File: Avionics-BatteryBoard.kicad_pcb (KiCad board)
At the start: 4 copper layers, 90.2 x 95.9 mm, 148 parts, among them J1 Keystone-1048, J2 Keystone-1048, J3 Keystone-1042, J4 Keystone-1042, J5 Fuel Gauge Programming Header, J6 205338-0002, J7 205338-0004, J8 282834-4, J9 522711069, Q1 SIRA99DP-T1-GE3, Q10 SIRA99DP-T1-GE3, Q11 MBT2222ADW1T1, Q12 NX3008NBKS, Q13 MBT2222ADW1T1, Q14 NX3008NBKS, Q2 IRLML2803, Q3 SIRA99DP-T1-GE3, Q4 IRLML2803, Q5 SIRA99DP-T1-GE3, Q6 IRLML2803, Q7 SIRA99DP-T1-GE3, Q8 SIRA99DP-T1-GE3, Q9 SIRA99DP-T1-GE3, U1 S-8209AAA-T8T1U, U10 TLX9000, U2 S-8209AAA-T8T1U, U3 LTC4412xS6, U4 LTC4412xS6, U5 MAX17205, U6 D5V0P4UR6SO, U7 D5V0P4UR6SO, U8 TLX9000, U9 TLX9000

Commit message: More v3.2 updates
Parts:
- H1, H2, H3, H4: footprint MountingHole:MountingHole_3.2mm_M3_Pad_TopBottom -> MountingHole:MountingHole_3.2mm_M3_Pad_Via
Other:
- outline, holes or cut-outs redrawn
- board text added: "TR"

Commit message: temporary changes
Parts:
- removed D1, D2: BAT60JFILM, Diode_SMD:D_SOD-323_HandSoldering
- removed F1, F2, F3, F4, F5, F6: 5A, Fuse:Fuse_1206_3216Metric
- removed J1, J2: Keystone-1048, Argus-Misc:BAT_1048
- removed J3, J4: Keystone-1042, Argus-Misc:Keystone_1042
- removed R21, R22, R23, R34, R35, R36: 10R, Resistor_SMD:R_2512_6332Metric
- added D7: BAT60JFILM, Diode_SMD:D_SOD-323_HandSoldering, F.Cu at (205.7, 122.5)
- added D8: BAT60JFILM, Diode_SMD:D_SOD-323_HandSoldering, F.Cu at (205.7, 125.4)
- added F12: 5A, Fuse:Fuse_1206_3216Metric, F.Cu at (200.3, 122.7)
- added F13: 5A, Fuse:Fuse_1206_3216Metric, F.Cu at (200.3, 126.0)
- added F14: 5A, Fuse:Fuse_1206_3216Metric, F.Cu at (200.3, 129.3)
- added F15: 5A, Fuse:Fuse_1206_3216Metric, F.Cu at (200.3, 132.6)
- added J11: ~, Argus-Battery:21700_battery_holder_th, F.Cu at (214.7, 139.5)
- TH1, TH6: moved to F.Cu
- moved R30 73.3 mm to (107.1, 68.2), turned to -90 degrees
- moved R29 50.3 mm to (107.1, 84.7), turned to -90 degrees
- moved TH4 39.8 mm to (117.3, 46.5)
- moved R28 26.6 mm to (110.5, 101.1), turned to -90 degrees
- moved TH6 24.2 mm to (115.0, 43.0)
- moved TH5 23.5 mm to (116.8, 43.7)
- moved R17 4.93 mm to (164.0, 62.5)
- moved R16 4.53 mm to (148.5, 63.5)
- moved H1 3.81 mm to (176.5, 139.7)
- moved H2 3.81 mm to (104.1, 139.7)
- moved R31 3.71 mm to (121.5, 109.5)
- moved H3 1.27 mm to (176.5, 54.0)
- moved TH1 0.46 mm to (164.5, 127.0)
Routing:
- net Net-(TH4-Pad2): track 17.6 -> 0.00 mm
- net Net-(TH2-Pad2): track 17.6 -> 0.00 mm
- net Net-(R22-Pad1): track 9.96 -> 0.00 mm
- net Net-(R21-Pad1): track 9.96 -> 0.00 mm
- net Net-(R35-Pad1): track 9.96 -> 0.00 mm
- net Net-(R32-Pad1): track 9.96 -> 0.00 mm
- net Net-(R29-Pad1): track 9.96 -> 0.00 mm
- net Net-(R16-Pad1): track 9.96 -> 0.00 mm
- net Net-(R34-Pad1): track 9.96 -> 0.00 mm
- net Net-(R31-Pad1): track 9.96 -> 0.00 mm
- net Net-(R28-Pad1): track 9.96 -> 0.00 mm
- net Net-(R18-Pad1): track 9.96 -> 0.00 mm
- net Net-(R15-Pad1): track 9.96 -> 0.01 mm
- net Net-(R19-Pad1): track 9.91 -> 0.00 mm
- net SYSTEM_VSS: track 20.7 -> 12.0 mm, vias 39 -> 37
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- added copper zone on B.Cu, net (none)
- removed copper zone on F.Cu, net /Battery Bus Detection/BATT_M
- removed copper zone on F.Cu, net /Battery Bus Detection/BATT_N
- removed copper zone on F.Cu, net /Battery Bus Detection/BATT_P
- removed copper zone on F.Cu, net /Battery Temperature Protection/BatteryHeater1/V_HEATER
- removed copper zone on F.Cu, net Net-(F1-Pad1)
- removed copper zone on F.Cu, net Net-(F2-Pad1)
- removed copper zone on F.Cu, net Net-(F3-Pad1)
- removed copper zone on F.Cu, net Net-(F4-Pad1)
- removed copper zone on B.Cu, net Net-(J3-NEG)
- removed copper zone on B.Cu, net Net-(J4-POS)

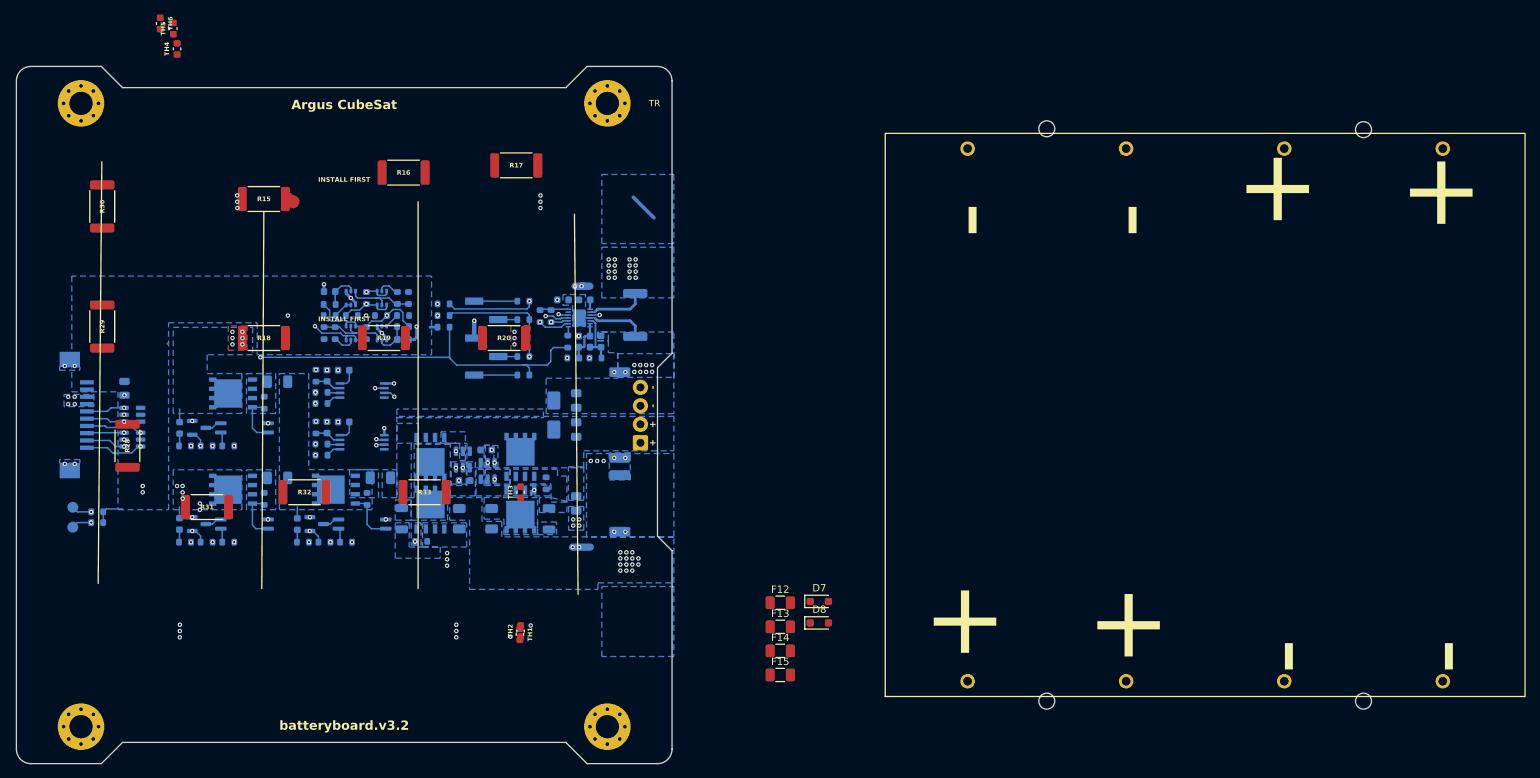
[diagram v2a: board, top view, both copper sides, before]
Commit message: deleting vias
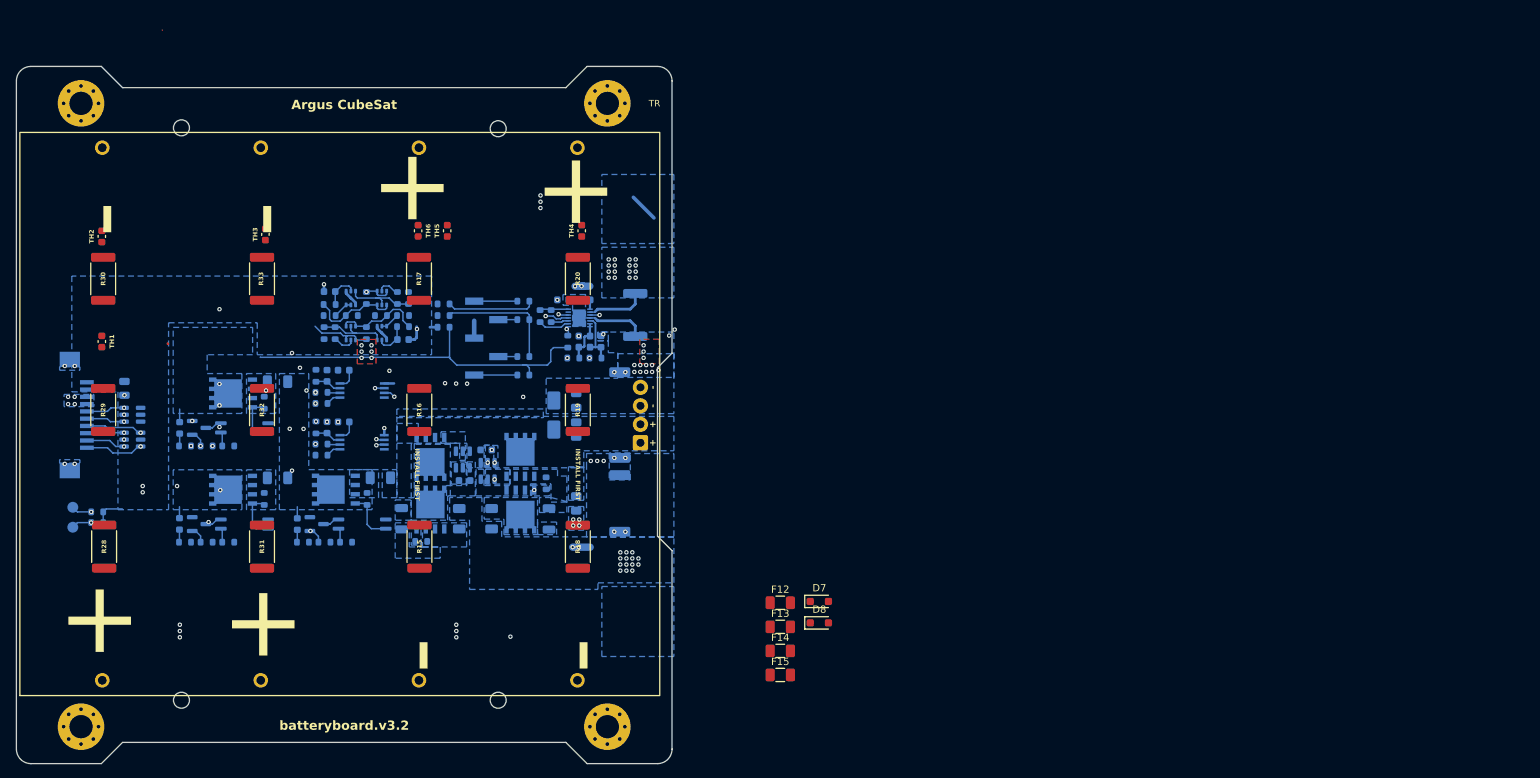
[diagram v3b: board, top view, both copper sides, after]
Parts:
- moved J11 119.0 mm to (95.7, 139.4)
- moved TH2 79.1 mm to (107.0, 72.3)
- moved TH1 70.2 mm to (107.0, 86.7)
- moved TH4 61.0 mm to (173.0, 71.5)
- moved R15 52.4 mm to (150.7, 114.9), turned to -90 degrees
- moved R18 51.8 mm to (172.5, 114.9), turned to -90 degrees
- moved TH3 49.9 mm to (129.5, 72.0)
- moved TH5 46.8 mm to (154.5, 71.5)
- moved TH6 45.5 mm to (150.5, 71.5)
- moved R33 36.9 mm to (129.0, 78.1), turned to -90 degrees
- moved R16 32.7 mm to (150.7, 96.1), turned to -90 degrees
- moved R19 28.4 mm to (172.5, 96.1), turned to -90 degrees
- moved R17 20.5 mm to (150.6, 78.1), turned to -90 degrees
- moved R28 14.2 mm to (107.3, 114.9)
- moved R20 13.0 mm to (172.5, 78.1), turned to -90 degrees
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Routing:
- net Net-(U5-AIN2): track 71.2 -> 2.43 mm, vias 2 -> 0
- net Net-(U5-AIN1): track 69.8 -> 4.37 mm, vias 1 -> 0
- net /Battery Temperature Protection/BatteryHeater1/V_HEATER: track 1.57 -> 67.0 mm, vias 9 -> 5
- net Net-(R19-Pad1): track 0.00 -> 2.28 mm, vias 0 -> 2
- net /Battery Bus Detection/BATT_M: track 5.66 -> 3.38 mm, vias 9 -> 6
- net VBUS: vias 0 -> 4
- net SYSTEM_VSS: vias 37 -> 25
- net Net-(U5-ALRT1): vias 0 -> 1
- net Net-(U1-CO): vias 2 -> 1
- net Net-(R32-Pad1): vias 0 -> 1
- net Net-(Q4-D): vias 0 -> 1
- net GND: vias 27 -> 26
- net /Interfaces/SDA_BUS: vias 2 -> 1
- net /Interfaces/SCL_BUS: vias 2 -> 3
- net /Interfaces/HEATER1_ON: vias 2 -> 1
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
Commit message: placed components start routing
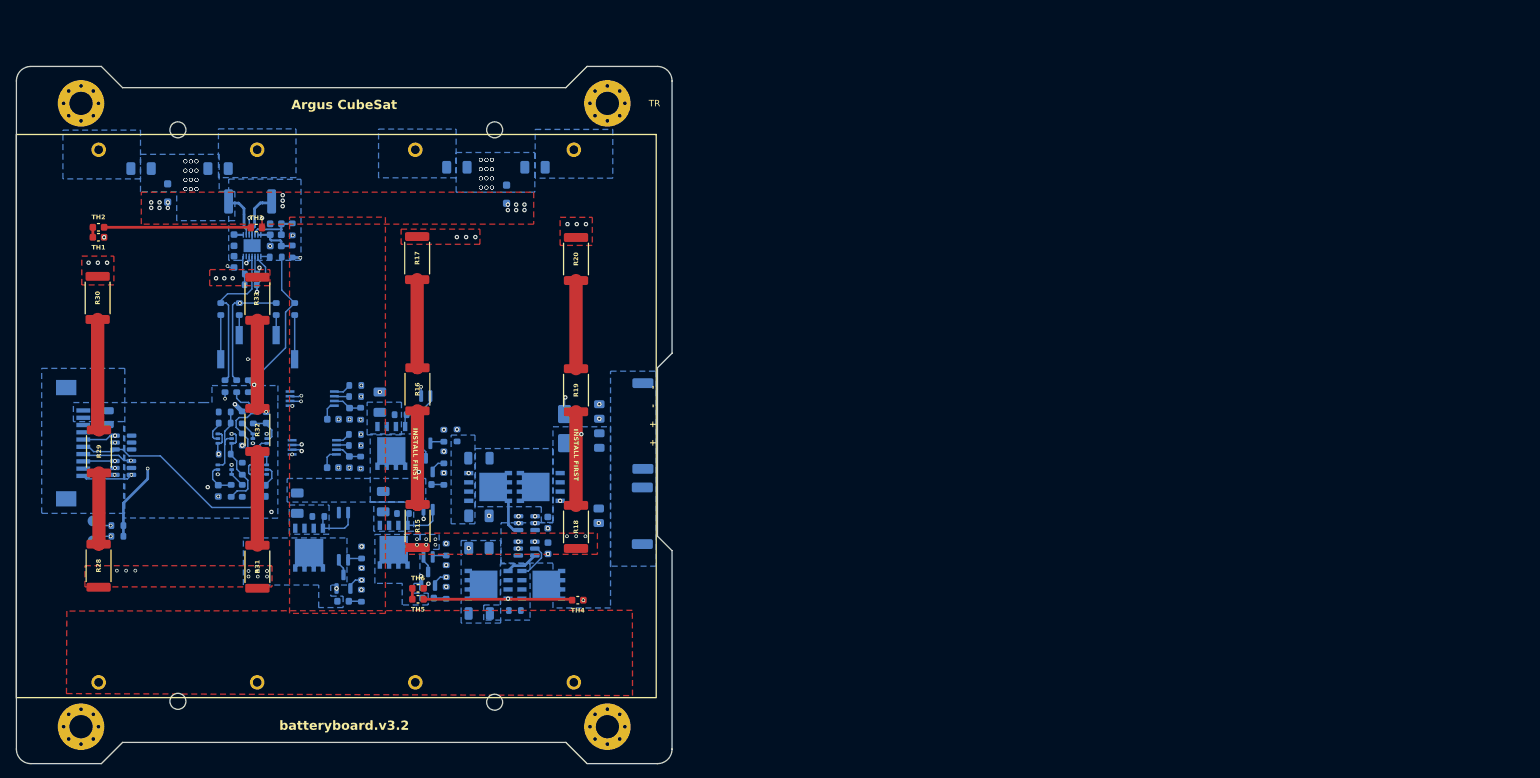
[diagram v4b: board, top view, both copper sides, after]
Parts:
- removed J8: 282834-4, TerminalBlock_TE-Connectivity:TerminalBlock_TE_282834-4_1x04_P2.54mm_Horizontal
- D7, D8, F12, F13, F14, F15: moved to B.Cu
- moved J11 122.0 mm to (183.2, 54.3), turned to -90 degrees
- moved F12 106.3 mm to (112.4, 62.9)
- moved D7 105.8 mm to (116.1, 66.3), turned to 90 degrees
- moved F13 99.8 mm to (123.0, 62.9), turned to 180 degrees
- moved F15 82.8 mm to (155.8, 62.8)
- moved F14 74.6 mm to (166.6, 62.8), turned to 180 degrees
- moved D8 73.0 mm to (162.7, 66.5), turned to -90 degrees
- moved R43 55.2 mm to (127.4, 67.5), turned to 180 degrees
- moved TH5 50.8 mm to (150.5, 122.2), turned to 180 degrees
- moved TH4 50.8 mm to (172.5, 122.3), turned to 180 degrees
- moved TH6 49.2 mm to (150.5, 120.7), turned to 0 degrees
- moved C11 48.9 mm to (125.2, 72.8), turned to -90 degrees
- moved C9 47.6 mm to (130.9, 70.5), turned to 180 degrees
- moved U5 46.1 mm to (127.7, 73.5), turned to -90 degrees
- moved C10 45.5 mm to (125.2, 75.8), turned to 90 degrees
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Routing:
- net Net-(U5-AIN1): track 4.37 -> 91.0 mm, vias 0 -> 2
- net /Battery Bus Protection/CHARGE_ACTIVE: track 71.3 -> 2.69 mm
- net /Battery Temperature Protection/BatteryHeater1/V_HEATER: track 67.0 -> 0.00 mm, vias 5 -> 9
- net /Battery Bus Protection/DISCHARGE_ACTIVE: track 69.7 -> 2.69 mm, vias 1 -> 2
- net /Interfaces/HEATER_ENABLE: track 43.9 -> 9.31 mm, vias 2 -> 1
- net /Interfaces/SCL_BUS: track 56.6 -> 23.7 mm, vias 3 -> 2
- net Net-(U5-AIN2): track 2.43 -> 34.7 mm, vias 0 -> 2
- net SYSTEM_VDD: track 0.00 -> 32.0 mm, vias 0 -> 2
- net /Interfaces/ALERT: track 84.9 -> 58.7 mm, vias 1 -> 2
- net /Interfaces/HEATER1_ON: track 30.3 -> 6.99 mm, vias 1 -> 2
- net Net-(TH4-Pad2): track 0.00 -> 20.5 mm
- net Net-(TH2-Pad2): track 0.00 -> 20.2 mm
- net /Battery Bus Detection/CHARGE_EN: track 33.4 -> 52.4 mm
- net /Interfaces/SDA_BUS: track 51.9 -> 35.9 mm, vias 1 -> 0
- net Net-(R29-Pad1): track 0.00 -> 15.3 mm
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- added copper zone on F.Cu, net /Battery Bus Detection/BATT_M
- added copper zone on F.Cu, net /Battery Temperature Protection/BatteryHeater1/V_HEATER
- added copper zone on B.Cu, net Net-(J11-neg3)
- added copper zone on B.Cu, net Net-(J11-neg4)
- added copper zone on B.Cu, net Net-(J11-pos1)
- added copper zone on B.Cu, net Net-(J11-pos2)
- removed copper zone on B.Cu, net (none)
- removed copper zone on B.Cu, net /Battery Bus Detection/CHARGE_EN
- removed copper zone on B.Cu, net /Battery Bus Detection/DISCHARGE_EN
- removed copper zone on B.Cu, net Net-(Q10-G)
- removed copper zone on B.Cu, net Net-(Q8-G)

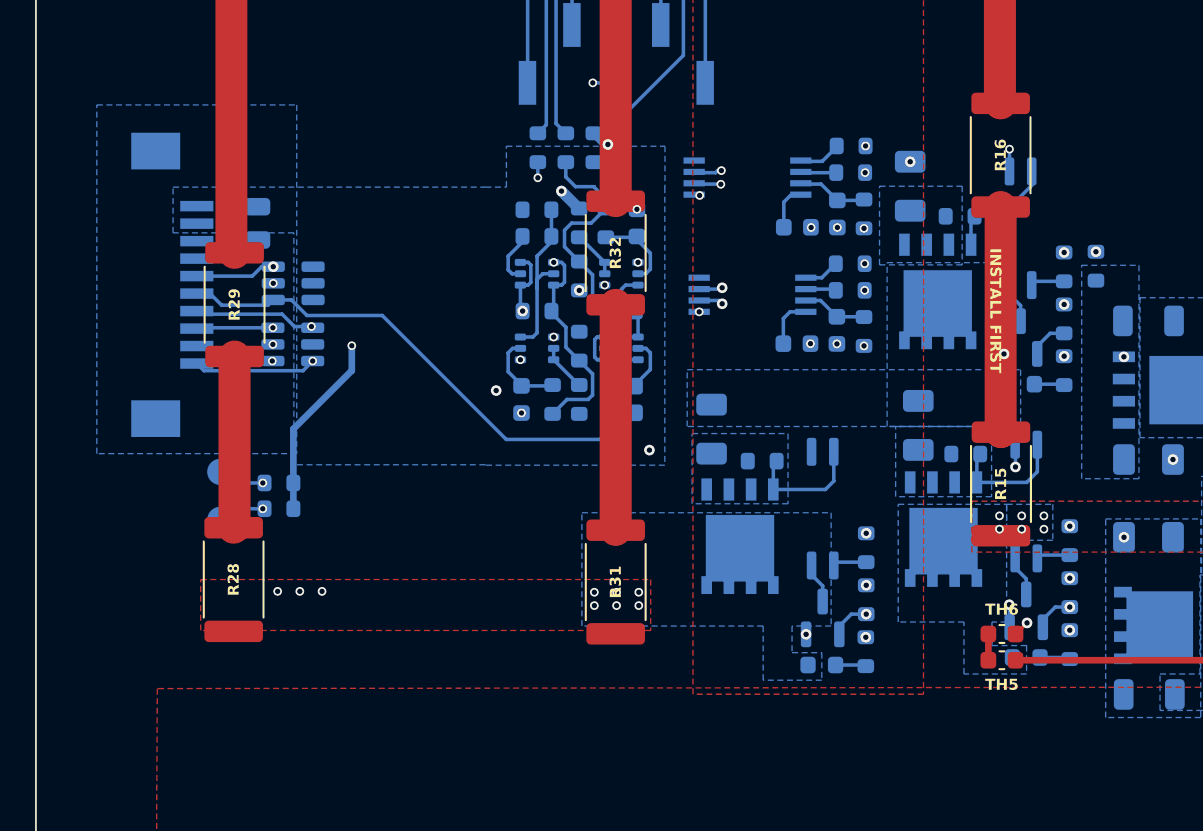
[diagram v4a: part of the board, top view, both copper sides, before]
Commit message: finished routing have to pass drc
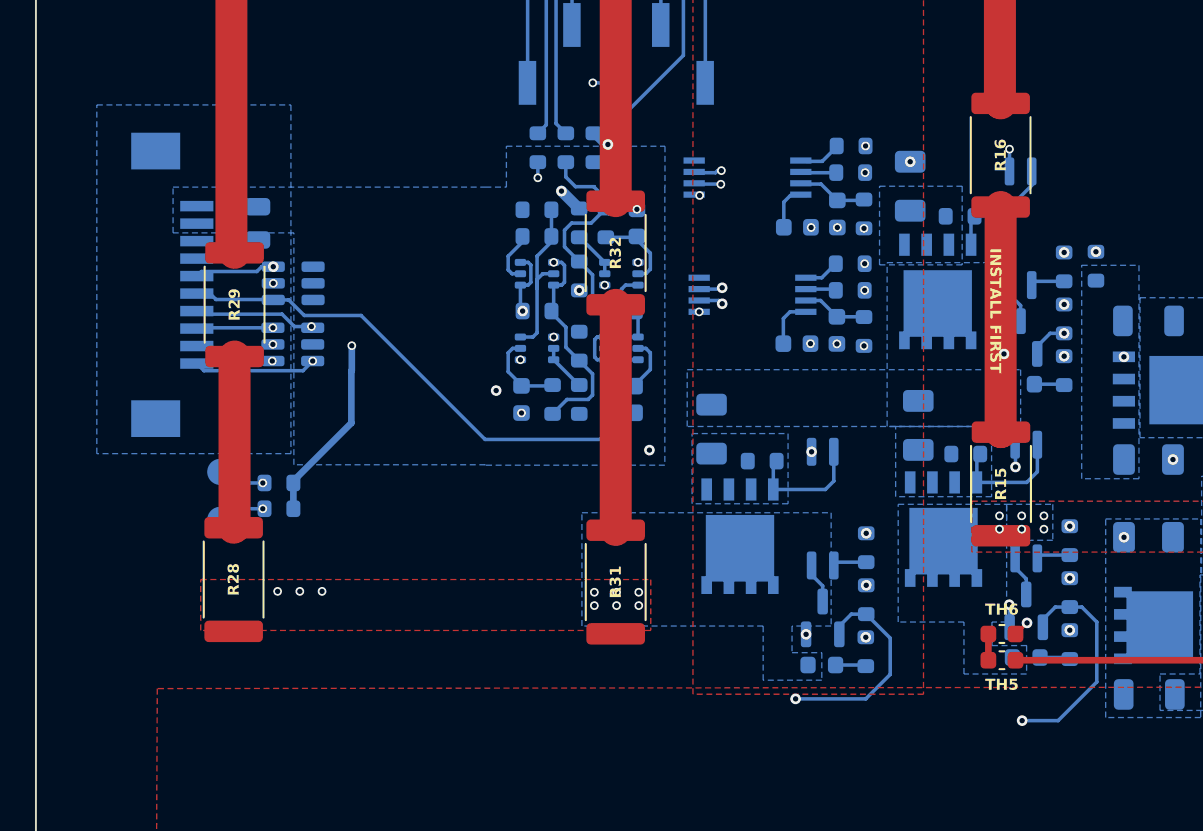
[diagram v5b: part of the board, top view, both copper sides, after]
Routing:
- net /Battery Bus Protection/DISCHARGE_ACTIVE: track 2.69 -> 119.1 mm
- net /Battery Bus Protection/CHARGE_ACTIVE: track 2.69 -> 101.5 mm
- net /Interfaces/HEATER0_ON: track 6.64 -> 73.5 mm
- net /Interfaces/HEATER1_ON: track 6.99 -> 54.9 mm
- net /Interfaces/HEATER_ENABLE: track 9.31 -> 55.9 mm, vias 1 -> 2
- net SYSTEM_VSS: vias 33 -> 34

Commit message: finishing up silksreen stuff
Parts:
- moved kibuzzard-67803442 30.6 mm to (105.5, 126.5)
- moved kibuzzard-67803551 28.2 mm to (109.2, 125.9), turned to 180 degrees
- moved kibuzzard-6780351B 25.1 mm to (92.6, 103.0), turned to 180 degrees
- moved kibuzzard-69DDC83B 4.03 mm to (101.6, 111.3)
- moved C14 1.32 mm to (109.2, 97.2)
- moved U6 1.24 mm to (111.2, 104.2)
- moved U7 1.14 mm to (111.1, 100.6)
- moved R51 0.29 mm to (127.4, 92.9)
- moved R32 0.10 mm to (128.4, 99.0)
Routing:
- net /Interfaces/HEATER1_ON: track 54.9 -> 64.4 mm
- net /Interfaces/HEATER0_ON: track 73.5 -> 81.4 mm
- net GND: track 1.30 -> 6.56 mm, vias 14 -> 32
- net /Battery Bus Protection/CHARGE_ACTIVE: track 101.5 -> 103.2 mm
- net Net-(TH4-Pad2): track 20.5 -> 21.6 mm
- net /Battery Bus Detection/BATT_N: track 6.19 -> 7.07 mm
- net /Battery Bus Detection/CHARGE_EN: track 52.4 -> 53.3 mm
- net /Interfaces/HEATER_ENABLE: track 55.9 -> 56.7 mm
- net SYSTEM_VDD: track 32.0 -> 32.6 mm
- net +3V3: track 79.4 -> 78.9 mm, vias 8 -> 9

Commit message: finished first draft of prototype
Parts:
- removed kibuzzard-67803442: G***, kibuzzard-67803442
- removed kibuzzard-6780351B: G***, kibuzzard-6780351B
- removed kibuzzard-67803551: G***, kibuzzard-67803551
- removed kibuzzard-69DDC83B: G***, kibuzzard-69DDC83B
- added kibuzzard-6A6B646A: G***, kibuzzard-6A6B646A, B.Cu at (101.7, 111.5)
- moved kibuzzard-6786F69C 1.32 mm to (101.7, 114.2)
- moved TH1 0.15 mm to (106.5, 72.5)
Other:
- board text added: "batteryboard.v4.0"
- board text removed: "batteryboard.v3.2"

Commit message: added changes
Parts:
- moved R29 1.52 mm to (106.5, 100.3)
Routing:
- net Net-(R29-Pad1): track 15.3 -> 14.1 mm
- net Net-(R28-Pad1): track 9.81 -> 10.7 mm
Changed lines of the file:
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@@
 	(footprint "Resistor_SMD:R_2512_6332Metric"
 		(layer "F.Cu")
-		(at 106.605633 101.845688 -90)
+		(at 106.4768 100.33 -90)
 		(descr "Resistor SMD 2512 (6332 Metric), square (rectangular) end terminal, IPC-7351 nominal, (Body size source: IPC-SM-782 page 72, https://www.pcb-3d.com/wordpress/wp-content/uploads/ipc-sm-782a_amendment_1_and_2.pdf), generated with kicad-footprint-generator")
 		(tags "resistor")
@@
 	)
 	(segment
-		(start 106.605633 104.808188)
+		(start 106.605633 103.894633)
 		(end 106.605633 114.5452)
 		(width 1.8288)
@@
 		(net "Net-(R28-Pad1)")
 	)
+	(segment
+		(start 106.6038 103.8928)
+		(end 106.605633 103.894633)
+		(width 1.8288)
+		(layer "F.Cu")
+		(net "Net-(R28-Pad1)")
+	)
 	(via
 		(at 109.0676 118.237)
@@
 	(segment
 		(start 106.425833 83.692797)
-		(end 106.425833 98.703388)
-		(width 1.8288)
-		(layer "F.Cu")
-		(net "Net-(R29-Pad1)")
-	)
-	(segment
-		(start 106.425833 98.703388)
-		(end 106.605633 98.883188)
+		(end 106.425833 97.789833)
 		(width 1.8288)
 		(layer "F.Cu")
